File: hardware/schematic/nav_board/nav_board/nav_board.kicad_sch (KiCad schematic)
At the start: 7 parts, among them J1 Conn_01x04_Pin, SW1 SW_Push, SW2 SW_Push

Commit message: First version of Nav PCB
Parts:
- removed J1: Conn_01x04_Pin, TerminalBlock:TerminalBlock_MaiXu_MX126-5.0-04P_1x04_P5.00mm, symbol Connector:Conn_01x04_Pin
- removed R1, R2: R_US, Resistor_THT:R_Axial_DIN0207_L6.3mm_D2.5mm_P7.62mm_Horizontal, symbol Device:R_US
- removed SW1, SW2: SW_Push, TerminalBlock:TerminalBlock_MaiXu_MX126-5.0-02P_1x02_P5.00mm, symbol Switch:SW_Push
- removed U1: ~, DPV_Nav_Library:EyeSPI_Breakout, symbol New_Library:EyeSpi_Breakout
- added J1: Screw_Terminal_01x04, TerminalBlock:TerminalBlock_MaiXu_MX126-5.0-04P_1x04_P5.00mm, symbol Connector:Screw_Terminal_01x04
- added J2: Screw_Terminal_01x03, TerminalBlock:TerminalBlock_MaiXu_MX126-5.0-03P_1x03_P5.00mm, symbol Connector:Screw_Terminal_01x03
- added U1: ~, DPVNav Footprint Library:Adafruit Ultimate GPS, symbol MCU_Module:Adafruit_Ultimate_GPS
- added U2: ~, DPVNav Footprint Library:Pololu Altimu-10 v5, symbol MCU_Module:Pololu_Altimu-10_v5
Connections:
- net +5V: now also J1.3 (Pin_3), J2.1 (Pin_1), U1.2 (Vin), U2.2 (Vin)
- net GND: now also J1.4 (Pin_4), J2.3 (Pin_3), U1.3 (GND), U2.3 (GND)
- net at A1.14 (RX/IO16): now also U1.5 (TX)
- net at A1.15 (TX/IO17): now also U1.4 (RX)
- net at A1.17 (SDA/IO23): now also U2.4 (SDA)
- net at A1.18 (SCL/IO22): now also U2.5 (SCL)
- net at A1.5 (DAC2/A0): now also J1.1 (Pin_1)
- net at A1.6 (DAC1/A1): now also J1.2 (Pin_2)
- net at A1.7 (I34/A2): now also J2.2 (Pin_2)
- net 3V3: no longer names the net of A1.2 (3V3)
- net DC: no longer names the net of A1.21 (A8/IO15)
- net MOSI: no longer names the net of A1.11 (SCK/IO5)

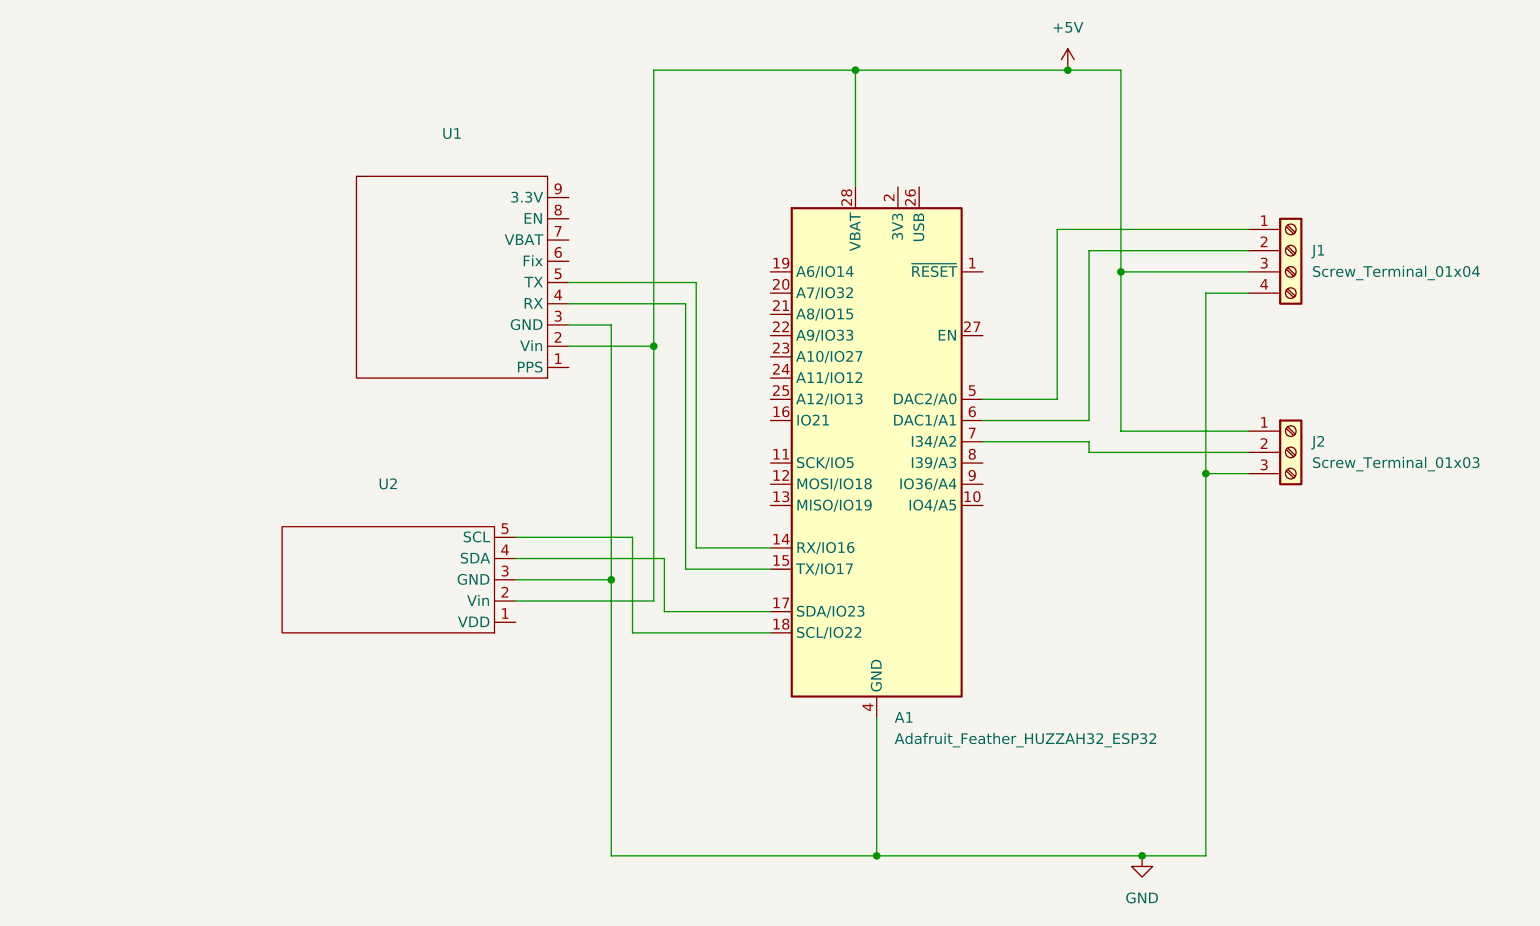
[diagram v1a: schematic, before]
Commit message: Updating nav board, and also K-factor for speed cal
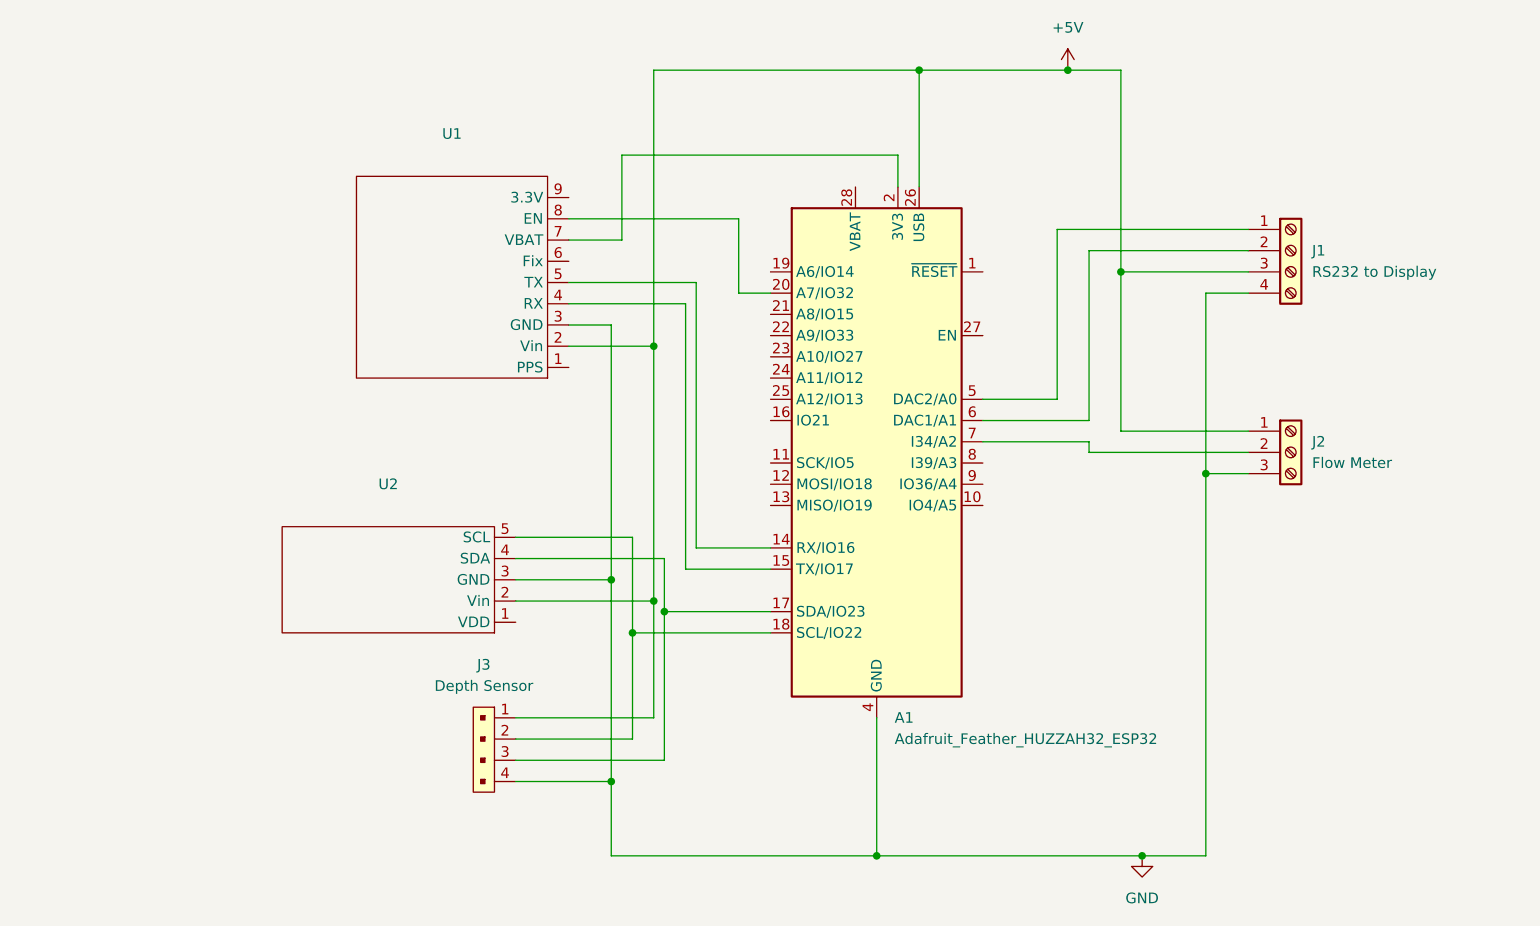
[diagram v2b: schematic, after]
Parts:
- added J3: Depth Sensor, Connector_Molex:Molex_PicoBlade_53047-0410_1x04_P1.25mm_Vertical, symbol dk_Rectangular-Connectors-Headers-Male-Pins:B4B-XH-A_LF__SN_
- J1: value Screw_Terminal_01x04 -> RS232 to Display; footprint TerminalBlock:TerminalBlock_MaiXu_MX126-5.0-04P_1x04_P5.00mm -> Connector_Molex:Molex_PicoBlade_53047-0410_1x04_P1.25mm_Vertical
- J2: value Screw_Terminal_01x03 -> Flow Meter; footprint TerminalBlock:TerminalBlock_MaiXu_MX126-5.0-03P_1x03_P5.00mm -> Connector_Molex:Molex_PicoBlade_53047-0310_1x03_P1.25mm_Vertical
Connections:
- net +5V: now also A1.26 (USB), J3.1; no longer A1.28 (VBAT)
- net GND: now also J3.4
- net at A1.17 (SDA/IO23), U2.4 (SDA): now also J3.3
- net at A1.18 (SCL/IO22), U2.5 (SCL): now also J3.2
- net at A1.2 (3V3): now also U1.7 (VBAT)
- net at A1.20 (A7/IO32): now also U1.8 (EN)
